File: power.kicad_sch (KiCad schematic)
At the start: 32 parts, among them U1 xc7z010clg400, U4 TPS621351, U5 TLV62130RGTT, U6 TLV62130RGTT, U7 SPX3819M5-L-3-3

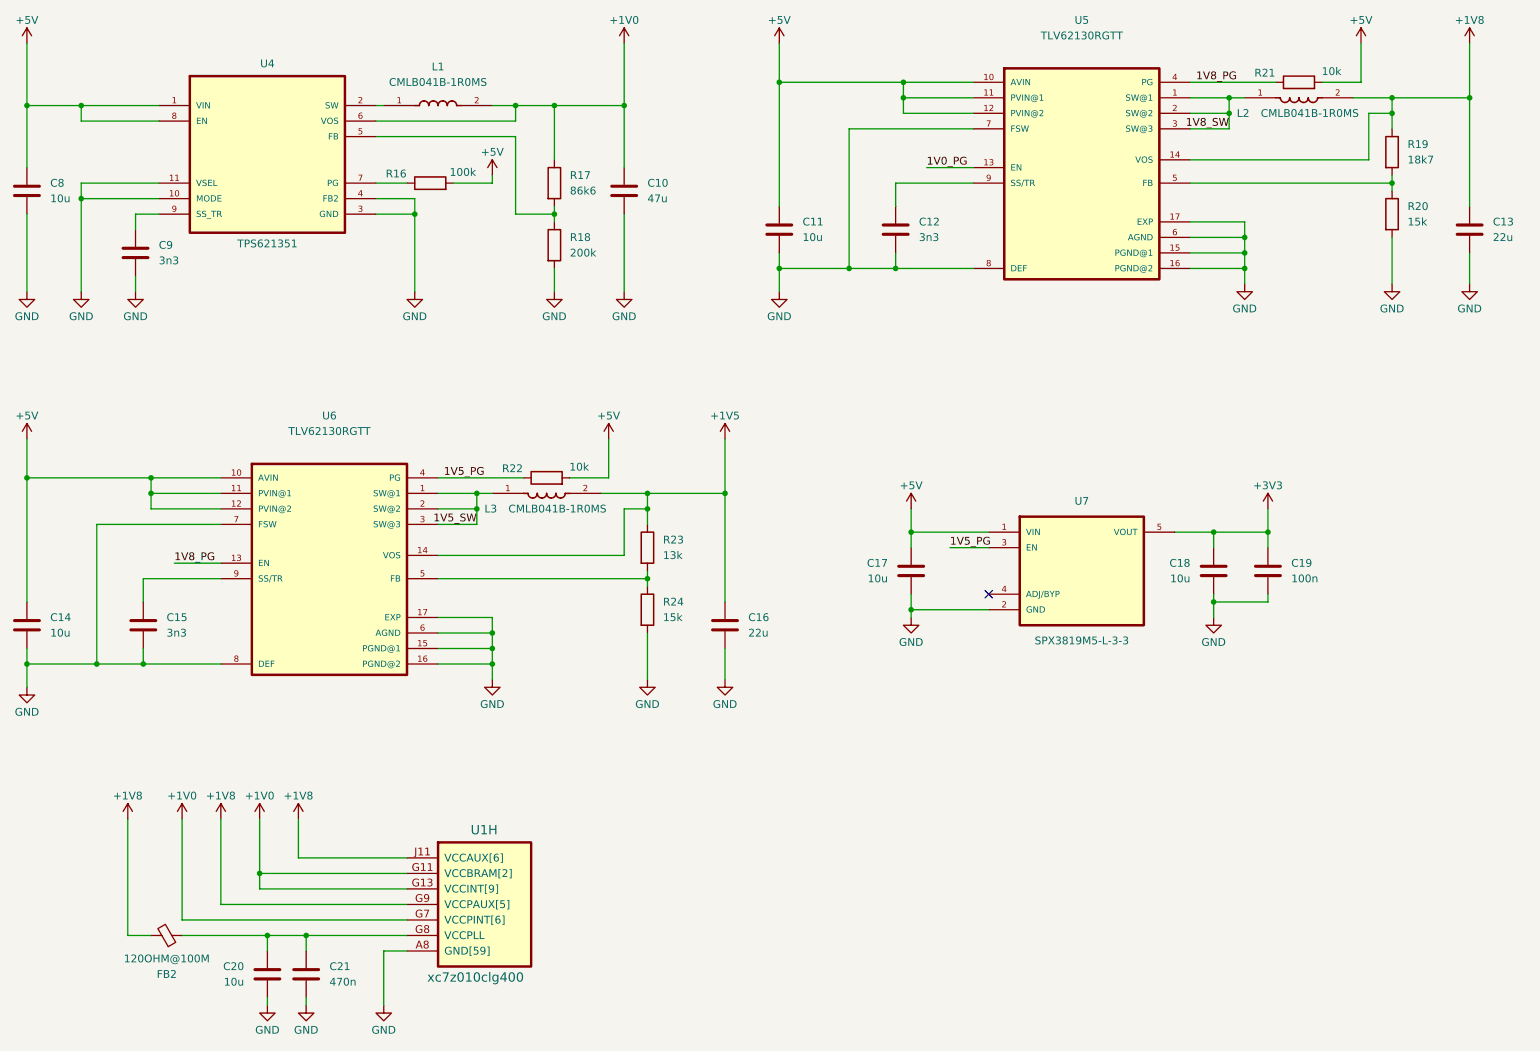
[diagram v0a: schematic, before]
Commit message: feat: finish ddr3 sch design
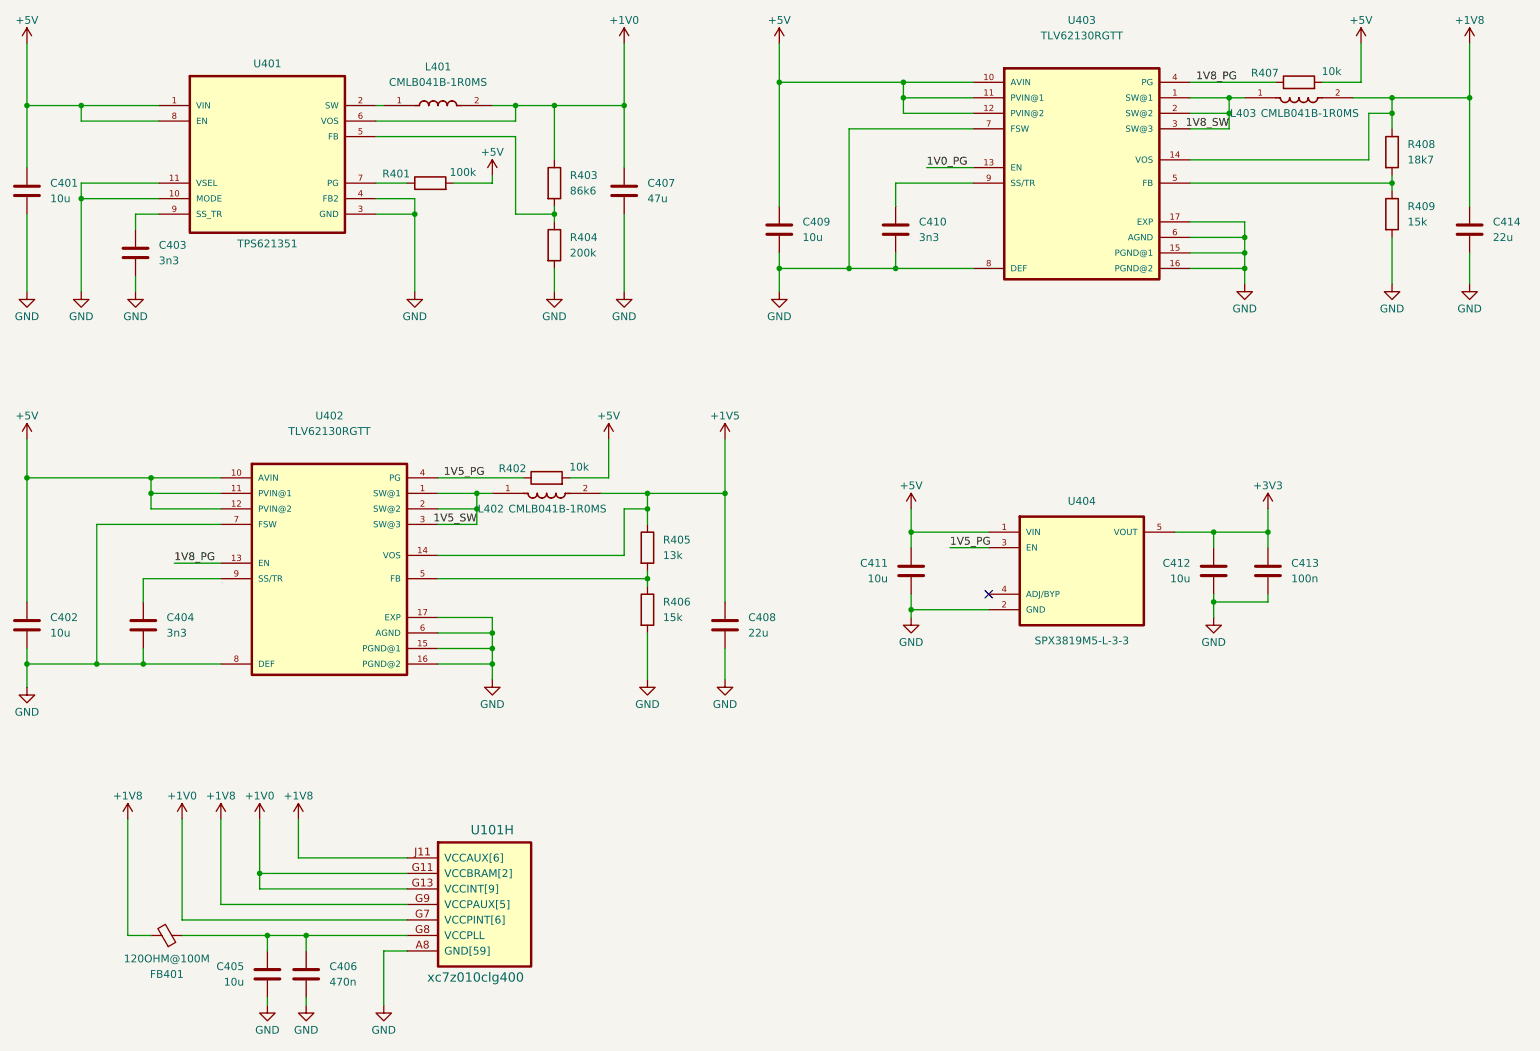
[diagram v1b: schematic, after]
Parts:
- renumbered C8 to C401, C14 to C402, C9 to C403, C15 to C404, C20 to C405, C21 to C406, C10 to C407, C16 to C408, C11 to C409, C12 to C410, C17 to C411, C18 to C412, C19 to C413, C13 to C414, FB2 to FB401, L1 to L401, L3 to L402, L2 to L403, R16 to R401, R22 to R402, R17 to R403, R18 to R404, R23 to R405, R24 to R406, R21 to R407, R19 to R408, R20 to R409, U1 to U101, U4 to U401, U6 to U402, U5 to U403, U7 to U404

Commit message: feat: start to routing DDR3
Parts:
- U101: footprint (none) -> Package_BGA:Xilinx_CLG400
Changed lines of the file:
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@@
 			)
 		)
-		(property "Footprint" ""
+		(property "Footprint" "Package_BGA:Xilinx_CLG400"
 			(at 24.13 153.67 0)
 			(hide yes)

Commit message: feat: restart routing ddr
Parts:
- C413: footprint (none) -> Capacitor_SMD:C_0402_1005Metric
- R402, R407: footprint (none) -> Resistor_SMD:R_0402_1005Metric
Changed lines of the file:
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@@
 			)
 		)
-		(property "Footprint" ""
+		(property "Footprint" "Capacitor_SMD:C_0402_1005Metric"
 			(at 229.5652 118.11 0)
 			(hide yes)
@@
 			)
 		)
-		(property "Footprint" ""
+		(property "Footprint" "Resistor_SMD:R_0402_1005Metric"
 			(at 110.49 100.838 90)
 			(hide yes)
@@
 			)
 		)
-		(property "Footprint" ""
+		(property "Footprint" "Resistor_SMD:R_0402_1005Metric"
 			(at 233.68 36.068 90)
 			(hide yes)
